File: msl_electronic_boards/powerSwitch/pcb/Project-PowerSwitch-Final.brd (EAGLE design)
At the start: 65.3 x 99.7 mm, 130 parts, among them IC10 BTS6133, IC11 BTS6133, IC12 BTS6133, IC15 BTS6133, IC3 LM2574M-5.0, IC4 BTS555E3146, IC7 MAX202, Q1 16Mhz, T1 BC847, T2 BC849, T5 BC849, T6 BC849, T7 BC849

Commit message: PCB PowerSwitch
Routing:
- net ICLED_KICK: track 89.0 -> 88.3 mm
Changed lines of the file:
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@@
 <wire x1="24.3" y1="28.768" x2="26.2255" y2="26.8425" width="0.254" layer="1"/>
 <wire x1="26.2255" y1="26.8425" x2="26.2255" y2="25.842" width="0.254" layer="1"/>
-<wire x1="46.04" y1="9.5885" x2="37.4015" y2="9.5885" width="0.254" layer="1"/>
-<wire x1="37.4015" y1="9.5885" x2="28.194" y2="18.796" width="0.254" layer="1"/>
-<wire x1="28.194" y1="18.796" x2="28.194" y2="23.8735" width="0.254" layer="1"/>
+<wire x1="46.04" y1="9.5885" x2="38.6715" y2="9.5885" width="0.254" layer="1"/>
+<wire x1="38.6715" y1="9.5885" x2="28.194" y2="20.066" width="0.254" layer="1"/>
+<wire x1="28.194" y1="20.066" x2="28.194" y2="23.8735" width="0.254" layer="1"/>
 <wire x1="28.194" y1="23.8735" x2="26.2255" y2="25.842" width="0.254" layer="1"/>
 <wire x1="24.3" y1="28.768" x2="24.196" y2="28.768" width="0.254" layer="1"/>
@@
 <contactref element="R27" pad="1"/>
 <contactref element="U$2" pad="28"/>
-<wire x1="46.04" y1="7.112" x2="38.862" y2="7.112" width="0.254" layer="1"/>
-<wire x1="38.862" y1="7.112" x2="25.4" y2="20.574" width="0.254" layer="1"/>
-<via x="25.4" y="20.574" extent="1-16" drill="0.8"/>
-<wire x1="25.4" y1="20.574" x2="20.574" y2="20.574" width="0.254" layer="16"/>
-<via x="20.574" y="20.574" extent="1-16" drill="0.8"/>
+<wire x1="46.04" y1="7.112" x2="39.878" y2="7.112" width="0.254" layer="1"/>
+<wire x1="39.878" y1="7.112" x2="25.654" y2="21.336" width="0.254" layer="1"/>
+<via x="25.654" y="21.336" extent="1-16" drill="0.8"/>
+<wire x1="25.654" y1="21.336" x2="19.812" y2="21.336" width="0.254" layer="16"/>
+<via x="19.812" y="21.336" extent="1-16" drill="0.8"/>
 <wire x1="19.5375" y1="28.6815" x2="19.2835" y2="28.6815" width="0.254" layer="1"/>
 <wire x1="18.288" y1="27.686" x2="16.51" y2="25.908" width="0.254" layer="1"/>
@@
 <wire x1="19.05" y1="64.008" x2="20.574" y2="65.532" width="0.254" layer="1"/>
 <via x="20.574" y="65.532" extent="1-16" drill="0.8"/>
-<wire x1="20.574" y1="20.574" x2="18.542" y2="22.606" width="0.254" layer="1"/>
+<wire x1="19.812" y1="21.336" x2="18.542" y2="22.606" width="0.254" layer="1"/>
 <wire x1="18.542" y1="22.606" x2="18.542" y2="23.622" width="0.254" layer="1"/>
 <wire x1="18.542" y1="23.622" x2="16.322" y2="25.842" width="0.254" layer="1"/>
@@
 <contactref element="R25" pad="1"/>
 <contactref element="U$2" pad="30"/>
-<wire x1="46.04" y1="4.572" x2="40.132" y2="4.572" width="0.254" layer="1"/>
-<wire x1="40.132" y1="4.572" x2="25.4" y2="19.304" width="0.254" layer="1"/>
-<via x="25.4" y="19.304" extent="1-16" drill="0.8"/>
-<wire x1="25.4" y1="19.304" x2="14.986" y2="19.304" width="0.254" layer="16"/>
-<via x="14.986" y="19.304" extent="1-16" drill="0.8"/>
-<wire x1="14.986" y1="19.304" x2="14.732" y2="19.558" width="0.254" layer="1"/>
-<wire x1="14.732" y1="19.558" x2="14.732" y2="24.572" width="0.254" layer="1"/>
+<wire x1="46.04" y1="4.572" x2="40.64" y2="4.572" width="0.254" layer="1"/>
+<wire x1="40.64" y1="4.572" x2="25.273" y2="19.685" width="0.254" layer="1"/>
+<via x="25.273" y="19.685" extent="1-16" drill="0.8"/>
+<wire x1="25.273" y1="19.685" x2="14.986" y2="19.685" width="0.254" layer="16"/>
+<via x="14.986" y="19.685" extent="1-16" drill="0.8"/>
+<wire x1="14.986" y1="19.685" x2="14.732" y2="19.939" width="0.254" layer="1"/>
+<wire x1="14.732" y1="19.939" x2="14.732" y2="24.572" width="0.254" layer="1"/>
 <wire x1="14.732" y1="24.572" x2="13.462" y2="25.842" width="0.254" layer="1"/>
 <wire x1="13.208" y1="27.686" x2="13.208" y2="26.096" width="0.254" layer="1"/>

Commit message: PCB PowerSwitch
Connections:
- net SW_12V: now also U$2.15
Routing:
- net SW_12V: track 12.4 -> 90.3 mm, vias 0 -> 4
- net ICLED_ROT: track 107.8 -> 106.0 mm
- net SW_KICK: track 101.0 -> 99.5 mm
- net SW_MOT: track 68.7 -> 68.1 mm

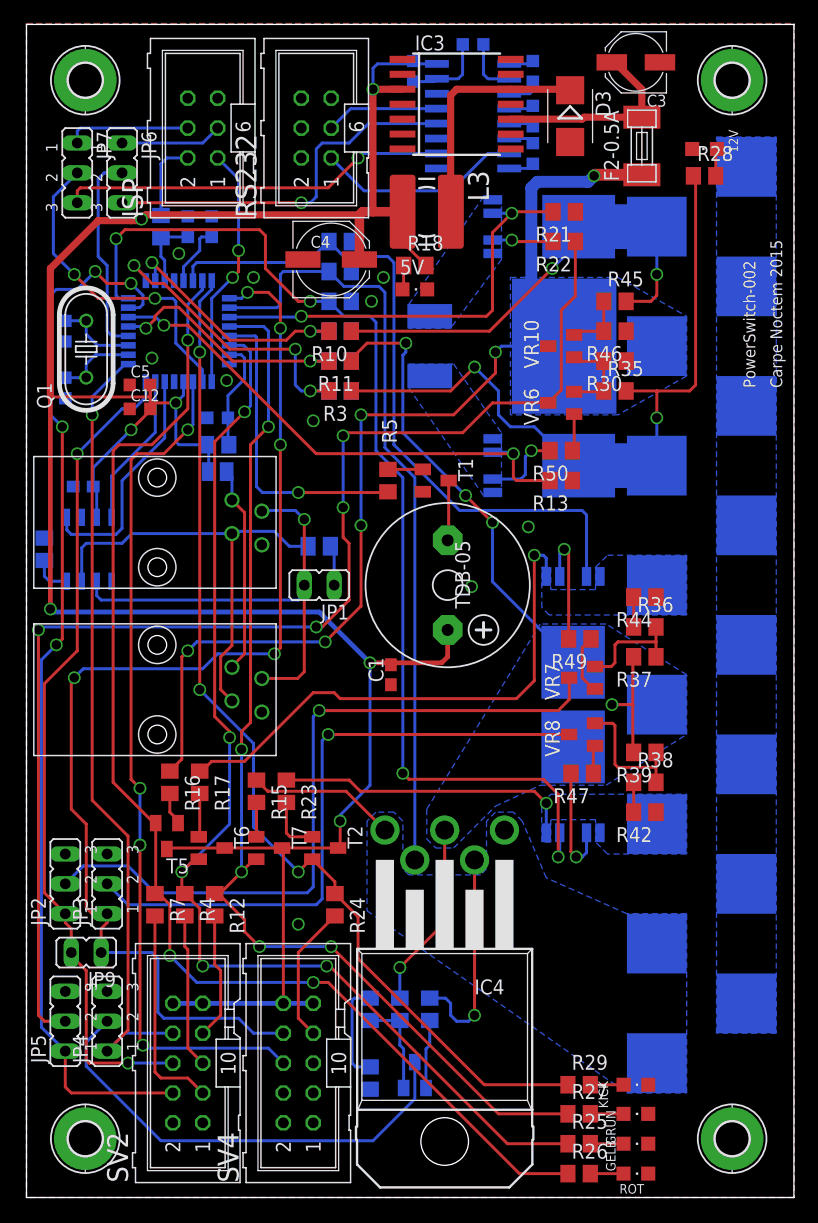
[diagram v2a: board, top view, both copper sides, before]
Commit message: PowerSwitch
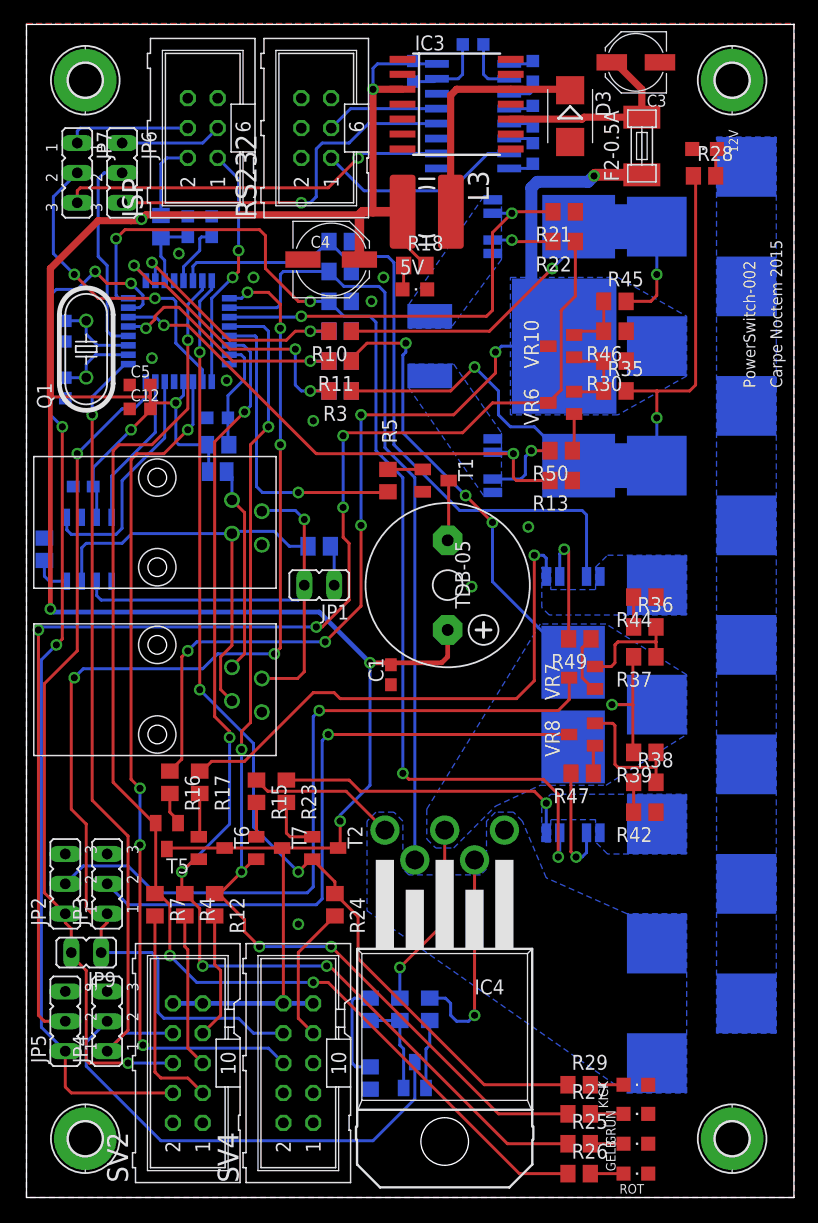
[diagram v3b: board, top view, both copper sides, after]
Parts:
- IC4: device infineon:TO220-52 -> micro-siemens:TO220-52
